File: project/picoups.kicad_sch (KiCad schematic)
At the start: 42 parts, among them J1 Conn_02x20_Odd_Even, J2 BATT, J3 VIN, J4 5V, Q1 Q_PMOS_GSD, U1 LT3652EMSE, U2 INA3221, U3 TPS61235P

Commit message: Semi final layout
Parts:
- J4: footprint Connector_JST:JST_PH_B2B-PH-K_1x02_P2.00mm_Vertical -> Connector_JST:JST_PH_S2B-PH-K_1x02_P2.00mm_Horizontal
- L1: footprint Inductor_SMD:L_Wuerth_HCI-1050 -> Inductor_SMD:L_Abracon_ASPI-4030S
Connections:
- net 5V: now also U2.1 (IN-3); no longer U2.11 (IN-1)
- net 5V+: now also U2.2 (IN+3); no longer U2.12 (IN+1)
- net RAW: now also U2.15 (IN+2); no longer U2.2 (IN+3)
- net VBAT: now also U2.12 (IN+1); no longer U2.15 (IN+2)
- net VBAT-: now also U2.11 (IN-1); no longer U2.14 (IN-2)
- net VIN: now also U2.14 (IN-2); no longer U2.1 (IN-3)

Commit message: Final version of this revision
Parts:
- C1, C4: footprint Capacitor_SMD:C_1206_3216Metric -> Capacitor_SMD:C_0805_2012Metric
- R7, R8, R9: value 0.005 -> 0.05
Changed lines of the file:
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@@
       (effects (font (size 1.27 1.27)))
     )
-    (property "Value" "0.005" (at 34.29 134.62 90)
+    (property "Value" "0.05" (at 34.29 134.62 90)
       (effects (font (size 1.27 1.27)))
     )
@@
       (effects (font (size 1.27 1.27)) (justify left))
     )
-    (property "Footprint" "Capacitor_SMD:C_1206_3216Metric" (at 23.8252 33.02 0)
+    (property "Footprint" "Capacitor_SMD:C_0805_2012Metric" (at 23.8252 33.02 0)
       (effects (font (size 1.27 1.27)) hide)
     )
@@
       (effects (font (size 1.27 1.27)))
     )
-    (property "Value" "0.005" (at 34.29 113.03 90)
+    (property "Value" "0.05" (at 34.29 113.03 90)
       (effects (font (size 1.27 1.27)))
     )
@@
       (effects (font (size 1.27 1.27)) (justify left))
     )
-    (property "Footprint" "Capacitor_SMD:C_1206_3216Metric" (at 36.5252 33.02 0)
+    (property "Footprint" "Capacitor_SMD:C_0805_2012Metric" (at 36.5252 33.02 0)
       (effects (font (size 1.27 1.27)) hide)
     )
@@
       (effects (font (size 1.27 1.27)))
     )
-    (property "Value" "0.005" (at 34.29 123.19 90)
-      (effects (font (size 1.27 1.27)))
-    )
+    (property "Value" "0.05" (at 34.29 123.19 90)
+      (effects (font (size 1.27 1.27)))
+    )

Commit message: Revision 1 single page
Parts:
- removed J4: 5V, Connector_JST:JST_PH_S2B-PH-K_1x02_P2.00mm_Horizontal, symbol Connector_Generic:Conn_01x02
- removed TP3: SDA, TestPoint:TestPoint_Pad_D2.0mm, symbol Connector:TestPoint
- removed TP4: SCL, TestPoint:TestPoint_Pad_D2.0mm, symbol Connector:TestPoint
- removed TP5: GND, TestPoint:TestPoint_Pad_D2.0mm, symbol Connector:TestPoint
- added C11, C9: 1uF, Capacitor_SMD:C_0805_2012Metric, symbol Device:C
- added D6: CHRG, LED_SMD:LED_0805_2012Metric, symbol Device:LED
- added D7: PWRGD, LED_SMD:LED_0805_2012Metric, symbol Device:LED
- added J5: USB_C_Receptacle, symbol Connector:USB_C_Receptacle
- added JP3: CHRG, Jumper:SolderJumper-2_P1.3mm_Open_RoundedPad1.0x1.5mm, symbol Jumper:SolderJumper_2_Open
- added JP4: PWRGD, Jumper:SolderJumper-2_P1.3mm_Open_RoundedPad1.0x1.5mm, symbol Jumper:SolderJumper_2_Open
- added R10: 1M, Resistor_SMD:R_1210_3225Metric, symbol Device:R
- added R12: 720, Resistor_SMD:R_0805_2012Metric, symbol Device:R
- added R13: 2k, Resistor_SMD:R_0805_2012Metric, symbol Device:R
- added R14, R15: 260, Resistor_SMD:R_0805_2012Metric, symbol Device:R
- added R16: 10k, Resistor_SMD:R_0805_2012Metric, symbol Device:R
- added R17, R18: 5.1k, Resistor_SMD:R_0805_2012Metric, symbol Device:R
- added SW1: SW_SPST, symbol Switch:SW_SPST
- added U4: M41T62, symbol PicoUPS:M41T62
- added U5: BQ24040, symbol PicoUPS:BQ24040
- added U6: TPS2116, symbol PicoUPS:TPS2116
- JP1: value FAULT_EN -> FAULT
- JP2: value CHRG_EN -> CHRG
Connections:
- net 5V: now also J1.2 (Pin_2), J1.4 (Pin_4); no longer C7.1, U2.4 (VS)
- net 5V+: now also C7.1, U2.4 (VS)
- net CHRG: now also JP3.1 (A), U5.8 (~{CHG})
- net GND: now also J1.14 (Pin_14), J1.20 (Pin_20), J1.25 (Pin_25), J1.30 (Pin_30), J1.34 (Pin_34), J1.39 (Pin_39), J1.6 (Pin_6), J1.9 (Pin_9), C11.1, C9.2, J5.A1 (GND), J5.A12 (GND), J5.B1 (GND), J5.B12 (GND), R10.1, R12.1, R13.1, R16.1, R17.1, R18.1, U4.3 (VSS), U5.3 (VSS), U5.7 (ISET2), U6.1 (GND); no longer U3.8 (INACT)
- net VBAT: now also SW1.1 (A), U4.5 (VCC), U6.2 (VOUT), U6.7 (VOUT); no longer C4.1, C5.1, C6.1, D1.2 (A), R1.2, R2.1, U1.9 (BAT), U3.7 (EN)
- net SCL: now reaches U2.6 (SCL)
- net SCL: now also J1.5 (Pin_5), U4.8 (SCL)
- net SDA: now reaches U2.7 (SDA)
- net SDA: now also J1.3 (Pin_3), U4.1 (SDA)
- net at R3.1, R4.2: now also R2.1; no longer R2.2
- net TIMER: no longer names the net of C3.1, U1.6 (TIMER)
- net VFB: no longer names the net of R4.1, U1.7 (V_{FB})
- new net: D6.1 (K), JP3.2 (B)
- new net: D6.2 (A), R14.1
- new net: J5.B5 (CC2), R18.2
- new net: R10.2, SW1.2 (B), U3.7 (EN)
- new net: R13.2, U5.4 (PRE-TERM)
- new net: J5.A5 (CC1), R17.2
- new net: R12.2, U5.2 (ISET)
- new net: R16.2, U5.9 (TS)
- new net: D7.1 (K), JP4.2 (B)
- new net: D7.2 (A), R15.1
- new net PWRGD: JP4.1 (A), U5.5 (~{PG})
- new net USB5V: C11.2, J5.A4 (VBUS), J5.A9 (VBUS), J5.B4 (VBUS), J5.B9 (VBUS), U5.1 (IN)
- new net VBAT_SOL: C4.1, C5.1, C6.1, D1.2 (A), R1.2, R2.2, U1.9 (BAT), U6.6 (VIN2)
- new net VBAT_USB: C9.1, R14.2, R15.2, U5.10 (OUT), U6.3 (VIN1), U6.4 (PR1), U6.5 (MODE)
- no-connect marks 45 -> 52
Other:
- note added: "5V SUPPLY"
- note added: "GPIO HEADER"
- note added: "POWER IO"
- note added: "POWER MONITOR"
- note added: "POWER MUX"
- note added: "RTC"
- note added: "SOLAR INPUT"
- note added: "STATUS LEDS"
- note added: "USB INPUT"
- note removed: "5V Boost Converter"
- note removed: "IO"
- note removed: "MPPT Battery Charger"
- note removed: "Power monitor"
- title: (none) -> PicoUPS
- moved on the sheet: C1, C10, C2, C3, C4, C5, C6, C7, C8, D1, D2, D3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

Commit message: Revision 1 multi-page
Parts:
- removed C1, C4, C8: 10uF, Capacitor_SMD:C_0805_2012Metric, symbol Device:C
- removed C10, C7: 22uF, Capacitor_SMD:C_0805_2012Metric, symbol Device:C
- removed C11, C2, C3, C9: 1uF, Capacitor_SMD:C_0805_2012Metric, symbol Device:C
- removed C5, C6: 47uF, Capacitor_SMD:C_1210_3225Metric, symbol Device:C
- removed D1, D2: 30V@3A, Diode_SMD:D_SOD-123F, symbol Device:D_Schottky
- removed D3, D6: CHRG, LED_SMD:LED_0805_2012Metric, symbol Device:LED
- removed D4: FAULT, LED_SMD:LED_0805_2012Metric, symbol Device:LED
- removed D7: PWRGD, LED_SMD:LED_0805_2012Metric, symbol Device:LED
- removed JP1: FAULT, Jumper:SolderJumper-2_P1.3mm_Open_RoundedPad1.0x1.5mm, symbol Jumper:SolderJumper_2_Open
- removed JP2, JP3: CHRG, Jumper:SolderJumper-2_P1.3mm_Open_RoundedPad1.0x1.5mm, symbol Jumper:SolderJumper_2_Open
- removed JP4: PWRGD, Jumper:SolderJumper-2_P1.3mm_Open_RoundedPad1.0x1.5mm, symbol Jumper:SolderJumper_2_Open
- removed L1: 8uH, Inductor_SMD:L_Abracon_ASPI-4030S, symbol Device:L
- removed L2: 1uH, Inductor_SMD:L_Vishay_IHLP-2020, symbol Device:L
- removed R1: 0.066, Resistor_SMD:R_0805_2012Metric, symbol Device:R
- removed R10: 1M, Resistor_SMD:R_1210_3225Metric, symbol Device:R
- removed R12: 720, Resistor_SMD:R_0805_2012Metric, symbol Device:R
- removed R13: 2k, Resistor_SMD:R_0805_2012Metric, symbol Device:R
- removed R14, R15, R5, R6: 260, Resistor_SMD:R_0805_2012Metric, symbol Device:R
- removed R16: 10k, Resistor_SMD:R_0805_2012Metric, symbol Device:R
- removed R2: 80k, Resistor_SMD:R_0805_2012Metric, symbol Device:R
- removed R3: 330k, Resistor_SMD:R_0805_2012Metric, symbol Device:R
- removed R4: 185k, Resistor_SMD:R_0805_2012Metric, symbol Device:R
- removed RV1: 10k, PicoUPS:Potentiometer_Bourns_3214G_Horizontal, symbol Device:R_Potentiometer
- removed SW1: SW_SPST, symbol Switch:SW_SPST
- removed TP1: VIN_REG, TestPoint:TestPoint_Pad_D2.0mm, symbol Connector:TestPoint
- removed TP2: GND, TestPoint:TestPoint_Pad_D2.0mm, symbol Connector:TestPoint
- removed U1: LT3652EMSE, Package_SO:MSOP-12-1EP_3x4mm_P0.65mm_EP1.65x2.85mm, symbol Battery_Management:LT3652EMSE
- removed U2: INA3221, Package_DFN_QFN:Texas_RGV_S-PVQFN-N16_EP2.1x2.1mm, symbol Power_Management:INA3221
- removed U3: TPS61235P, PicoUPS:TPS61235P, symbol PicoUPS:TPS61235P
- removed U5: BQ24040, symbol PicoUPS:BQ24040
- removed U6: TPS2116, symbol PicoUPS:TPS2116
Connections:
- net VBAT-: now also R8.1; no longer R8.2
- net RAW renamed Solar Panel Supply/VIN
- net Solar Panel Supply/VIN: no longer R7.1
- net USB5V renamed USB_5V
- net VBAT renamed VBAT+
- net VBAT+: now also R8.2; no longer R8.1
- net VIN renamed VBAT_SOL-
- new net VBAT_SOL+: R7.1
- no-connect marks 52 -> 45
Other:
- added sheet 5V Power Supply (5v_power_supply.kicad_sch)
- added sheet Power Monitor (power_monitor.kicad_sch)
- added sheet Power Mux (power_mux.kicad_sch)
- added sheet Solar Panel Supply (solar_panel_supply.kicad_sch)
- added sheet Status LEDs (status_leds.kicad_sch)
- added sheet USB Power Supply (usb_power_supply.kicad_sch)
- note removed: "5V SUPPLY"
- note removed: "GPIO HEADER"
- note removed: "POWER IO"
- note removed: "POWER MONITOR"
- note removed: "POWER MUX"
- note removed: "RTC"
- note removed: "SOLAR INPUT"
- note removed: "STATUS LEDS"
- note removed: "USB INPUT"
- moved on the sheet: D5, J1, J3, J5, Q1, R11, R17, R18, U4

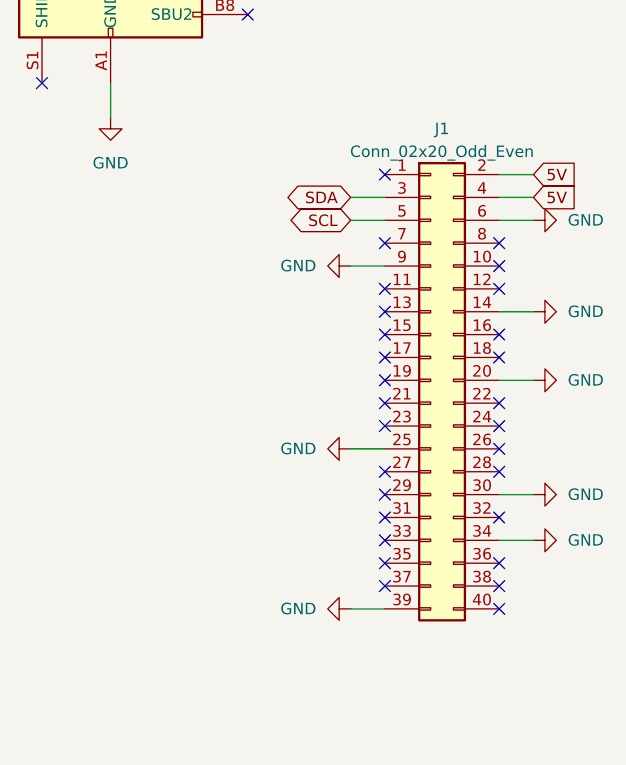
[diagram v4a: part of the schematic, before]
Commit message: Added user button
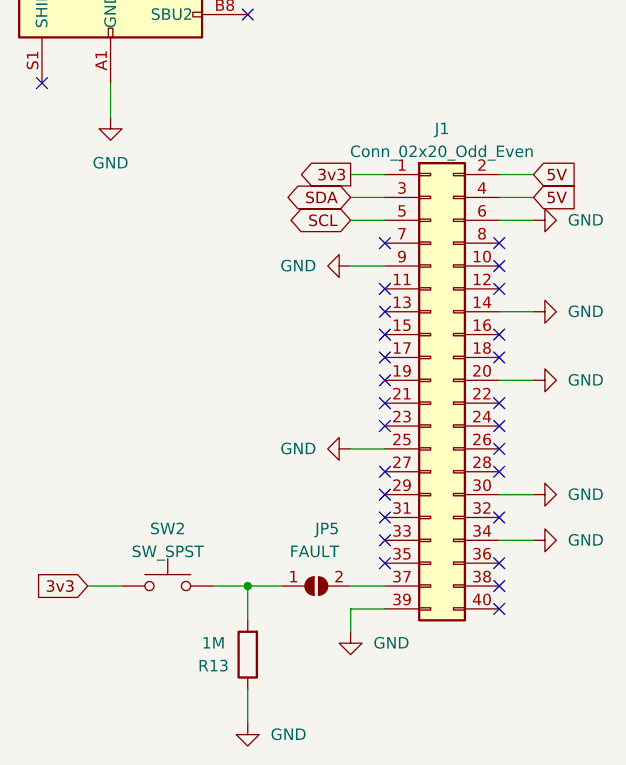
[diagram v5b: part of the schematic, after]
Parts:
- added JP5: FAULT, Jumper:SolderJumper-2_P1.3mm_Open_RoundedPad1.0x1.5mm, symbol Jumper:SolderJumper_2_Open
- added R13: 1M, Resistor_SMD:R_1210_3225Metric, symbol Device:R
- added SW2: SW_SPST, symbol Switch:SW_Push
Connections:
- net GND: now also R13.1
- net 3v3: now reaches J1.1 (Pin_1)
- net 3v3: now also SW2.1
- net at J1.37 (Pin_37): now also JP5.2 (B)
- new net: JP5.1 (A), R13.2, SW2.2
- no-connect marks 45 -> 43
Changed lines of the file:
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@@
   (junction (at 205.74 41.91) (diameter 0) (color 0 0 0 0)
+  )
+  (junction (at 45.72 152.4) (diameter 0) (color 0 0 0 0)
   )
   (no_connect (at 45.72 81.28))
@@
   (no_connect (at 45.72 71.12))
   (no_connect (at 73.66 144.78))
+  (no_connect (at 60.96 127))
   (no_connect (at 45.72 55.88))
   (no_connect (at 73.66 132.08))
   (no_connect (at 73.66 139.7))
   (no_connect (at 22.86 96.52))
-  (no_connect (at 60.96 127))
   (no_connect (at 45.72 50.8))
   (no_connect (at 60.96 149.86))
@@
   (no_connect (at 60.96 144.78))
   (no_connect (at 60.96 121.92))
-  (no_connect (at 60.96 152.4))
   (no_connect (at 73.66 149.86))
   (no_connect (at 45.72 48.26))
   (no_connect (at 45.72 73.66))
-  (no_connect (at 60.96 106.68))
   (no_connect (at 45.72 86.36))
   (no_connect (at 73.66 137.16))
@@
     (stroke (width 0) (type default))
   )
+  (wire (pts (xy 57.15 152.4) (xy 60.96 152.4))
+    (stroke (width 0) (type default))
+  )
   (wire (pts (xy 73.66 147.32) (xy 77.47 147.32))
     (stroke (width 0) (type default))
@@
     (stroke (width 0) (type default))
   )
+  (wire (pts (xy 45.72 156.21) (xy 45.72 152.4))
+    (stroke (width 0) (type default))
+  )
+  (wire (pts (xy 45.72 163.83) (xy 45.72 167.64))
+    (stroke (width 0) (type default))
+  )
   (wire (pts (xy 271.78 41.91) (xy 274.32 41.91))
     (stroke (width 0) (type default))
@@
     (stroke (width 0) (type default))
   )
+  (wire (pts (xy 41.91 152.4) (xy 45.72 152.4))
+    (stroke (width 0) (type default))
+  )
   (wire (pts (xy 205.74 41.91) (xy 205.74 66.04))
     (stroke (width 0) (type default))
@@
     (stroke (width 0) (type default))
   )
+  (wire (pts (xy 57.15 154.94) (xy 57.15 157.48))
+    (stroke (width 0) (type default))
+  )
   (wire (pts (xy 97.79 43.18) (xy 110.49 43.18))
     (stroke (width 0) (type default))
@@
     (stroke (width 0) (type default))
   )
+  (wire (pts (xy 57.15 106.68) (xy 60.96 106.68))
+    (stroke (width 0) (type default))
+  )
   (wire (pts (xy 57.15 109.22) (xy 60.96 109.22))
     (stroke (width 0) (type default))
@@
   )
   (wire (pts (xy 138.43 97.79) (xy 142.24 97.79))
+    (stroke (width 0) (type default))
+  )
+  (wire (pts (xy 45.72 152.4) (xy 49.53 152.4))
+    (stroke (width 0) (type default))
+  )
+  (wire (pts (xy 27.94 152.4) (xy 31.75 152.4))
     (stroke (width 0) (type default))
   )
@@
     )
   )
+  (global_label "3v3" (shape output) (at 57.15 106.68 180) (fields_autoplaced)
+    (effects (font (size 1.27 1.27)) (justify right))
+    (property "Intersheetrefs" "${INTERSHEET_REFS}" (at 50.8576 106.68 0)
+      (effects (font (size 1.27 1.27)) (justify right) hide)
+    )
+  )
   (global_label "5V+" (shape input) (at 106.68 97.79 180) (fields_autoplaced)
     (effects (font (size 1.27 1.27)) (justify right))
@@
     )
   )
+  (global_label "3v3" (shape input) (at 27.94 152.4 180) (fields_autoplaced)
+    (effects (font (size 1.27 1.27)) (justify right))
+    (property "Intersheetrefs" "${INTERSHEET_REFS}" (at 21.6476 152.4 0)
+      (effects (font (size 1.27 1.27)) (justify right) hide)
+    )
+  )
   (global_label "5V" (shape output) (at 274.32 41.91 0) (fields_autoplaced)
     (effects (font (size 1.27 1.27)) (justify left))
@@
         (path "/d62f1157-7c2f-4dce-8167-d5624900d267"
           (reference "#PWR029") (unit 1)
+        )
+      )
+    )
+  )
+  (symbol (lib_id "power:GND") (at 45.72 167.64 0) (unit 1)
+    (in_bom yes) (on_board yes) (dnp no) (fields_autoplaced)
+    (property "Reference" "#PWR031" (at 45.72 173.99 0)
+      (effects (font (size 1.27 1.27)) hide)
+    )
+    (property "Value" "GND" (at 48.26 168.91 0)
+      (effects (font (size 1.27 1.27)) (justify left))
+    )
+    (property "Footprint" "" (at 45.72 167.64 0)
+      (effects (font (size 1.27 1.27)) hide)
+    )
+    (property "Datasheet" "" (at 45.72 167.64 0)
+      (effects (font (size 1.27 1.27)) hide)
+    )
+    (pin "1")
+    (instances
+      (project "picoups"
+        (path "/d62f1157-7c2f-4dce-8167-d5624900d267"
+          (reference "#PWR031") (unit 1)
         )
       )
@@
     )
   )
+  (symbol (lib_id "Jumper:SolderJumper_2_Open") (at 53.34 152.4 0) (mirror x) (unit 1)
+    (in_bom yes) (on_board yes) (dnp no)
+    (property "Reference" "JP5" (at 55.88 146.05 0)
+      (effects (font (size 1.27 1.27)) (justify right))
+    )
+    (property "Value" "FAULT" (at 55.88 148.59 0)
+      (effects (font (size 1.27 1.27)) (justify right))
+    )
+    (property "Footprint" "Jumper:SolderJumper-2_P1.3mm_Open_RoundedPad1.0x1.5mm" (at 53.34 152.4 0)
+      (effects (font (size 1.27 1.27)) hide)
+    )
+    (property "Datasheet" "~" (at 53.34 152.4 0)
+      (effects (font (size 1.27 1.27)) hide)
+    )
+    (pin "1")
+    (pin "2")
+    (instances
+      (project "picoups"
+        (path "/d62f1157-7c2f-4dce-8167-d5624900d267"
+          (reference "JP5") (unit 1)
+        )
+        (path "/d62f1157-7c2f-4dce-8167-d5624900d267/e21d3221-edd3-4144-8d1a-91b5737dd9b8"
+          (reference "JP1") (unit 1)
+        )
+      )
+    )
+  )
   (symbol (lib_id "power:GND") (at 57.15 137.16 270) (unit 1)
     (in_bom yes) (on_board yes) (dnp no) (fields_autoplaced)
@@
     )
   )
-  (symbol (lib_id "power:GND") (at 57.15 154.94 270) (unit 1)
-    (in_bom yes) (on_board yes) (dnp no) (fields_autoplaced)
-    (property "Reference" "#PWR026" (at 50.8 154.94 0)
-      (effects (font (size 1.27 1.27)) hide)
-    )
-    (property "Value" "GND" (at 53.34 154.94 90)
-      (effects (font (size 1.27 1.27)) (justify right))
-    )
-    (property "Footprint" "" (at 57.15 154.94 0)
-      (effects (font (size 1.27 1.27)) hide)
-    )
-    (property "Datasheet" "" (at 57.15 154.94 0)
+  (symbol (lib_id "Switch:SW_Push") (at 36.83 152.4 0) (unit 1)
+    (in_bom yes) (on_board yes) (dnp no) (fields_autoplaced)
+    (property "Reference" "SW2" (at 36.83 146.05 0)
+      (effects (font (size 1.27 1.27)))
+    )
+    (property "Value" "SW_SPST" (at 36.83 148.59 0)
+      (effects (font (size 1.27 1.27)))
+    )
+    (property "Footprint" "" (at 36.83 147.32 0)
+      (effects (font (size 1.27 1.27)) hide)
+    )
+    (property "Datasheet" "~" (at 36.83 147.32 0)
+      (effects (font (size 1.27 1.27)) hide)
+    )
+    (pin "1")
+    (pin "2")
+    (instances
+      (project "picoups"
+        (path "/d62f1157-7c2f-4dce-8167-d5624900d267"
+          (reference "SW2") (unit 1)
+        )
+        (path "/d62f1157-7c2f-4dce-8167-d5624900d267/92ed0473-53e9-4211-a651-f912f1c2bd2b"
+          (reference "SW1") (unit 1)
+        )
+      )
+    )
+  )
+  (symbol (lib_id "power:GND") (at 57.15 157.48 0) (unit 1)
+    (in_bom yes) (on_board yes) (dnp no) (fields_autoplaced)
+    (property "Reference" "#PWR026" (at 57.15 163.83 0)
+      (effects (font (size 1.27 1.27)) hide)
+    )
+    (property "Value" "GND" (at 59.69 158.75 0)
+      (effects (font (size 1.27 1.27)) (justify left))
+    )
+    (property "Footprint" "" (at 57.15 157.48 0)
+      (effects (font (size 1.27 1.27)) hide)
+    )
+    (property "Datasheet" "" (at 57.15 157.48 0)
       (effects (font (size 1.27 1.27)) hide)
     )
@@
         )
       )
+    )
+  )
+  (symbol (lib_id "Device:R") (at 45.72 160.02 180) (unit 1)
+    (in_bom yes) (on_board yes) (dnp no)
+    (property "Reference" "R13" (at 41.91 161.29 0)
+      (effects (font (size 1.27 1.27)))
+    )
+    (property "Value" "1M" (at 41.91 158.75 0)
+      (effects (font (size 1.27 1.27)))
+    )
+    (property "Footprint" "Resistor_SMD:R_1210_3225Metric" (at 47.498 160.02 90)
+      (effects (font (size 1.27 1.27)) hide)
+    )
+    (property "Datasheet" "~" (at 45.72 160.02 0)
+      (effects (font (size 1.27 1.27)) hide)
+    )
+    (pin "1")
+    (pin "2")
+    (instances
+      (project "picoups"
+        (path "/d62f1157-7c2f-4dce-8167-d5624900d267"
+          (reference "R13") (unit 1)
+        )
+        (path "/d62f1157-7c2f-4dce-8167-d5624900d267/92ed0473-53e9-4211-a651-f912f1c2bd2b"
+          (reference "R4") (unit 1)
+        )
+      )
